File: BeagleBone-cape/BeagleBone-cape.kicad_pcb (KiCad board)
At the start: 4 copper layers, 86.4 x 54.6 mm, 102 parts, among them IC1 A6983C50QTR, IC2 TCAN3413DDFR, IC3 BMP390, J1 Servo 0, J10 MotorR, J11 CAN, J12 24V, J13 MAVLink, J2 Servo 1, J3 Servo 2, J4 Servo 3, J5 LEDL, J6 LEDR, J8 Air Speed Sensor, J9 MotorL, P8 BeagleBone_Black_Header, P9 BeagleBone_Black_Header, Q1 DMP3013SFV, Q2 Q_NMOS_GSD, U1 IIS2MDC, U2 LSM6DSV16X, U3 DS1307ZN+, U4 LSM6DSV16X, U6 LTC4412ES6, Y1 32.768kHz

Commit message: Cape: unify CAN/FDCAN net names in schematic; ISSUES: ERC/DRC status update
Co-Authored-By: Claude Sonnet 5.5 <noreply@anthropic.com>
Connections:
- net /CAN+ renamed /CANH
- net /CAN- renamed /CANL
- P9 pad 14: /IMU_INT2 -> /IMU_INT1
- P9 pad 16: /IMU_INT1 -> /IMU_INT2
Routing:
- net /PGOOD: track 5.02 -> 52.3 mm
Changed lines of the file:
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@@
 	(net 66 "Net-(D1-A)")
 	(net 67 "Net-(D2-A)")
-	(net 68 "/CAN-")
-	(net 69 "/CAN+")
+	(net 68 "/CANL")
+	(net 69 "/CANH")
 	(net 70 "Net-(IC1-VCC)")
 	(net 71 "Net-(IC1-VINLDO)")
@@
 			(layers "*.Cu" "*.Mask")
 			(remove_unused_layers no)
-			(net 94 "/IMU_INT2")
+			(net 92 "/IMU_INT1")
 			(pinfunction "Pin_14")
 			(pintype "passive")
@@
 			(layers "*.Cu" "*.Mask")
 			(remove_unused_layers no)
-			(net 92 "/IMU_INT1")
+			(net 94 "/IMU_INT2")
 			(pinfunction "Pin_16")
 			(pintype "passive")
@@
 			(remove_unused_layers no)
 			(roundrect_rratio 0.125)
-			(net 69 "/CAN+")
+			(net 69 "/CANH")
 			(pinfunction "Pin_1")
 			(pintype "passive")
@@
 			(layers "*.Cu" "*.Mask")
 			(remove_unused_layers no)
-			(net 68 "/CAN-")
+			(net 68 "/CANL")
 			(pinfunction "Pin_2")
 			(pintype "passive")
@@
 			(size 0.45 1.2)
 			(layers "F.Cu" "F.Mask" "F.Paste")
-			(net 68 "/CAN-")
+			(net 68 "/CANL")
 			(pinfunction "CANL")
 			(pintype "passive")
@@
 			(size 0.45 1.2)
 			(layers "F.Cu" "F.Mask" "F.Paste")
-			(net 69 "/CAN+")
+			(net 69 "/CANH")
 			(pinfunction "CANH")
 			(pintype "passive")
@@
 			(layers "F.Cu" "F.Mask" "F.Paste")
 			(roundrect_rratio 0.25)
-			(net 68 "/CAN-")
+			(net 68 "/CANL")
 			(pinfunction "K")
 			(pintype "passive")
@@
 			(layers "F.Cu" "F.Mask" "F.Paste")
 			(roundrect_rratio 0.25)
-			(net 69 "/CAN+")
+			(net 69 "/CANH")
 			(pinfunction "K")
 			(pintype "passive")
@@
 			(size 1 1)
 			(layers "F.Cu" "F.Mask")
-			(net 68 "/CAN-")
+			(net 68 "/CANL")
 			(pinfunction "1")
 			(pintype "passive")
@@
 			(layers "F.Cu" "F.Mask" "F.Paste")
 			(roundrect_rratio 0.25)
-			(net 68 "/CAN-")
+			(net 68 "/CANL")
 			(pintype "passive")
 		)
@@
 			(layers "F.Cu" "F.Mask" "F.Paste")
 			(roundrect_rratio 0.25)
-			(net 69 "/CAN+")
+			(net 69 "/CANH")
 			(pintype "passive")
 		)
@@
 			(size 1 1)
 			(layers "F.Cu" "F.Mask")
-			(net 69 "/CAN+")
+			(net 69 "/CANH")
 			(pinfunction "1")
 			(pintype "passive")
@@
 		(net 101)
 	)
+	(segment
+		(start 123.71 48.58)
+		(end 131.32 48.58)
+		(width 0.25)
+		(layer "In2.Cu")
+		(net 101)
+	)
+	(segment
+		(start 123.49 48.8)
+		(end 123.71 48.58)
+		(width 0.25)
+		(layer "In2.Cu")
+		(net 101)
+	)
+	(segment
+		(start 132.52 47.38)
+		(end 132.5 47.38)
+		(width 0.25)
+		(layer "In2.Cu")
+		(net 101)
+	)
+	(segment
+		(start 121.46 79.15)
+		(end 121.46 54.78)
+		(width 0.25)
+		(layer "In2.Cu")
+		(net 101)
+	)
+	(segment
+		(start 131.32 48.58)
+		(end 132.52 47.38)
+		(width 0.25)
+		(layer "In2.Cu")
+		(net 101)
+	)
+	(segment
+		(start 118.31 82.3)
+		(end 121.46 79.15)
+		(width 0.25)
+		(layer "In2.Cu")
+		(net 101)
+	)
+	(segment
+		(start 123.49 52.75)
+		(end 123.49 48.8)
+		(width 0.25)
+		(layer "In2.Cu")
+		(net 101)
+	)
+	(segment
+		(start 121.46 54.78)
+		(end 123.49 52.75)
+		(width 0.25)
+		(layer "In2.Cu")
+		(net 101)
+	)
+	(segment
+		(start 118.31 84.27)
+		(end 118.31 82.3)
+		(width 0.25)
+		(layer "In2.Cu")
+		(net 101)
+	)

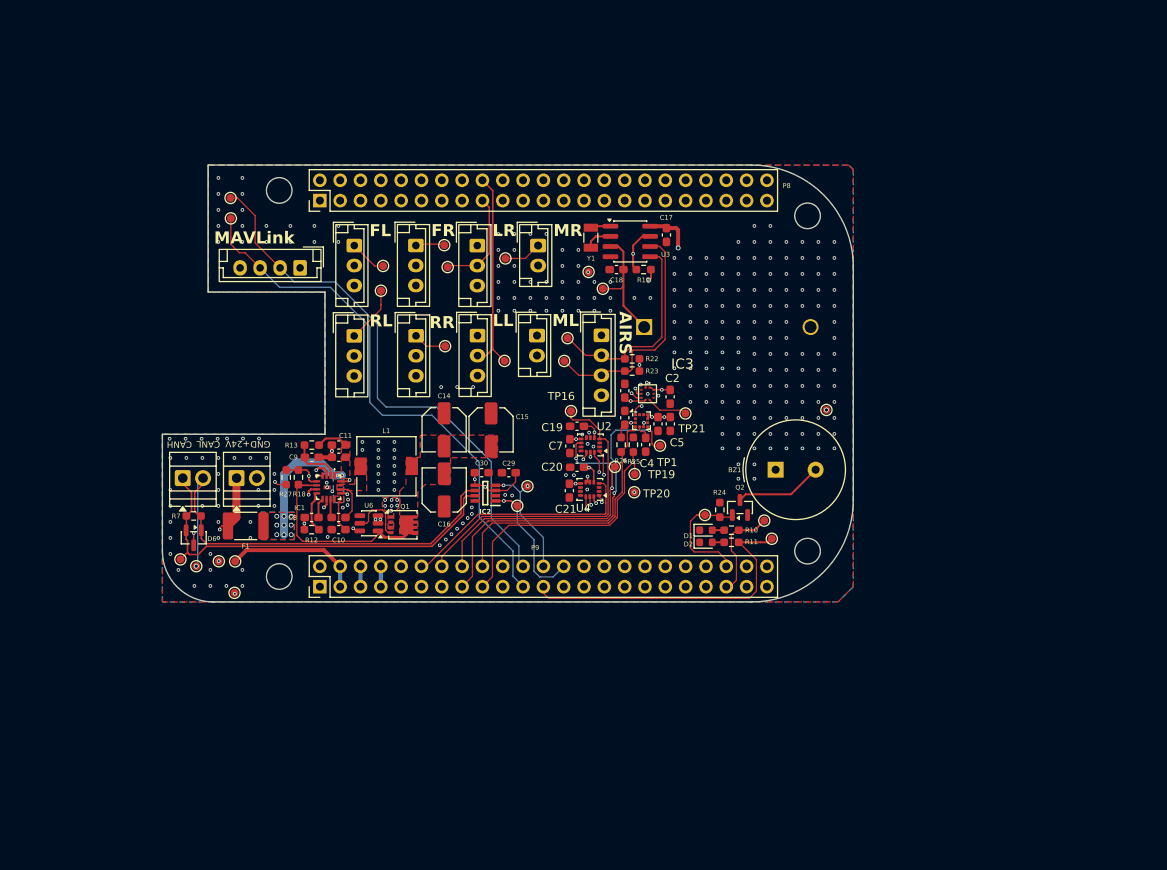
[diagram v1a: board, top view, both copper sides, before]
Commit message: WIP: Q3 -> S-LP03N060TZHG (SOT-223), PCB synced with new schematic parts, not yet routed (DRC: shorts, 200 unconnected)
Co-Authored-By: Claude Sonnet 5.5 <noreply@anthropic.com>
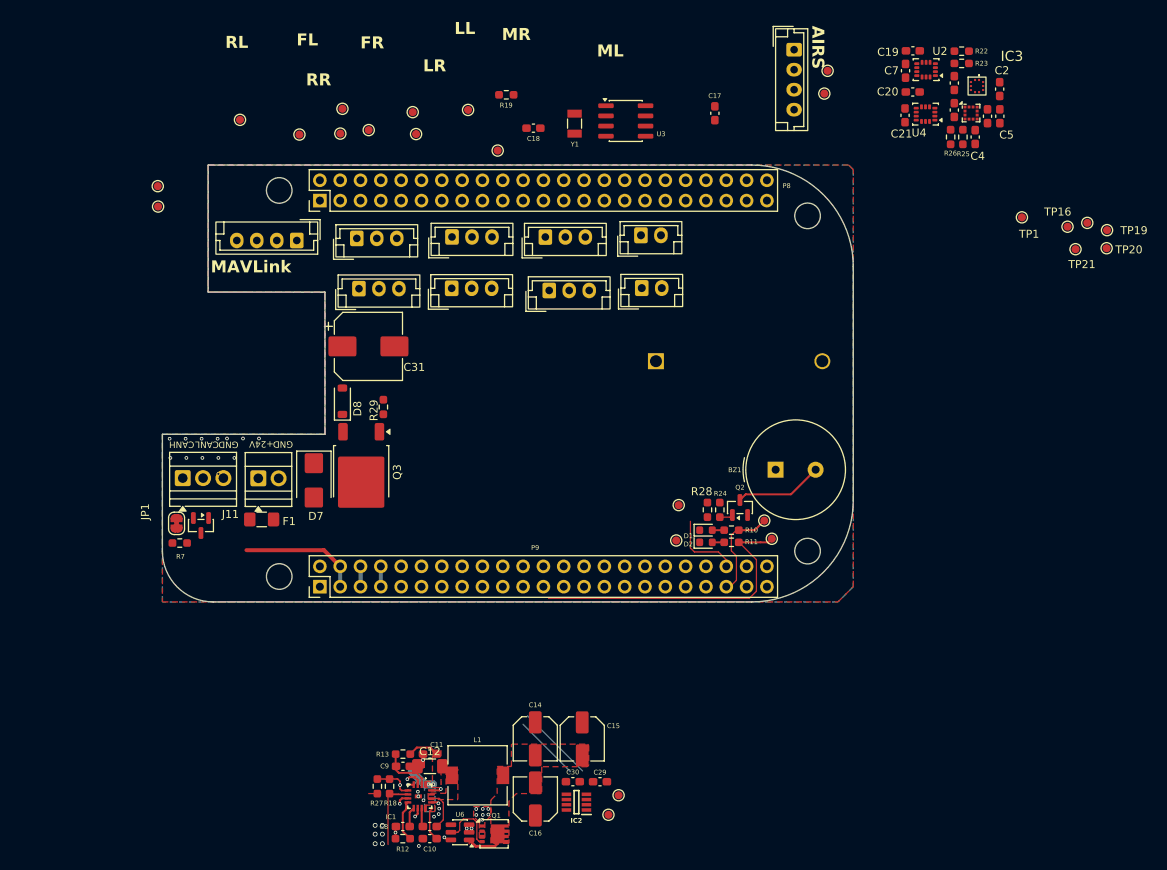
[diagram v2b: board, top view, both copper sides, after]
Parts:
- removed TP10, TP27, TP28, TP29, TP34: TestPoint, TestPoint:TestPoint_Pad_D1.0mm
- added C31: 100u 50V, Capacitor_SMD:CP_Elec_8x10, F.Cu at (125.8, 68.1)
- added D7: SMBJ33CA, Diode_SMD:D_SMB, F.Cu at (118.9, 84.8)
- added D8: BZT52C12, Diode_SMD:D_SOD-123, F.Cu at (122.5, 74.9)
- added JP1: CAN_TERM, Jumper:SolderJumper-2_P1.3mm_Bridged_RoundedPad1.0x1.5mm, F.Cu at (101.8, 90.2)
- added Q3: AOD4185L, Package_TO_SOT_SMD:TO-252-2, F.Cu at (124.8, 83.8)
- added R28: 1k, Resistor_SMD:R_0603_1608Metric_Pad0.98x0.95mm_HandSolder, F.Cu at (168.1, 88.5)
- added R29: 100k, Resistor_SMD:R_0603_1608Metric_Pad0.98x0.95mm_HandSolder, F.Cu at (127.6, 75.6)
- C12: value 10u -> 10u 50V; footprint Capacitor_SMD:C_0603_1608Metric_Pad1.08x0.95mm_HandSolder -> Capacitor_SMD:C_1206_3216Metric_Pad1.33x1.80mm_HandSolder
- F1: value Fuse -> 2A 63V; footprint Fuse:Fuse_1812_4532Metric_Pad1.30x3.40mm_HandSolder -> Fuse:Fuse_1206_3216Metric_Pad1.42x1.75mm_HandSolder
- J11: footprint TerminalBlock:TerminalBlock_Xinya_XY308-2.54-2P_1x02_P2.54mm_Horizontal -> TerminalBlock:TerminalBlock_Xinya_XY308-2.54-3P_1x03_P2.54mm_Horizontal
- J2: value Servo 1 -> Servo 2
- J3: value Servo 2 -> Servo 1
- R10: value 420 -> 100
- R11: value 420 -> 470
- moved TP17 66.5 mm to (215.6, 52.6)
- moved TP19 66.5 mm to (218.1, 53.5)
- moved TP20 66.5 mm to (218.0, 55.8)
- moved TP16 66.2 mm to (213.1, 53.1)
- moved C19 63.0 mm to (193.8, 31.1)
- moved C21 62.9 mm to (192.8, 39.2)
- moved C7 62.9 mm to (192.9, 33.6)
- moved U2 62.9 mm to (195.5, 33.5)
- moved C20 62.9 mm to (193.8, 36.3)
- moved U4 62.9 mm to (195.4, 39.0)
- moved IC3 56.4 mm to (201.8, 35.5)
- moved C1 56.4 mm to (199.0, 35.1)
- moved C2 56.4 mm to (204.7, 35.9)
- moved C3 56.4 mm to (203.1, 39.3)
- moved C4 56.4 mm to (201.6, 41.9)
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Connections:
- net /FDCAN_RX renamed /CAN_RX
- net /FDCAN_TX renamed /CAN_TX
- F1 pad 2: +24V -> /Power/VIN_F
- R7 pad 2: /CANH -> Net-(JP1-B)
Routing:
- net /SERVO_1: track 68.9 -> 0.00 mm
- net /I2C2.SCL: track 64.2 -> 0.00 mm
- net /SERVO_3: track 61.8 -> 0.00 mm
- net /UART_TX: track 68.9 -> 8.39 mm
- net /I2C2.SDA: track 59.2 -> 0.00 mm
- net /UART_RX: track 68.4 -> 9.70 mm
- net /CANL: track 58.5 -> 0.00 mm, vias 1 -> 0
- net /SERVO_0: track 52.4 -> 0.00 mm
- net /CANH: track 52.0 -> 0.00 mm
- net /I2C1.SDA: track 50.1 -> 0.00 mm, vias 3 -> 0
- net /I2C1.SCL: track 47.2 -> 0.00 mm, vias 3 -> 0
- net /SERVO_2: track 46.2 -> 0.00 mm
- net /PGOOD: track 52.3 -> 6.99 mm
- net /MAG_DRDY: track 44.5 -> 0.00 mm, vias 2 -> 0
- net /MOTOR_R: track 41.4 -> 0.00 mm
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
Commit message: WIP: snap servo/LED/motor connectors to 4x2 grid, further PCB and pwr sheet edits
Co-Authored-By: Claude Sonnet 5.5 <noreply@anthropic.com>
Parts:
- removed C12: 10u 50V, Capacitor_SMD:C_1206_3216Metric_Pad1.33x1.80mm_HandSolder
- added TP10: TestPoint, TestPoint:TestPoint_Pad_D1.0mm, F.Cu at (83.8, 79.9)
- added TP27: TestPoint, TestPoint:TestPoint_Pad_D1.0mm, F.Cu at (83.8, 82.9)
- added TP28: TestPoint, TestPoint:TestPoint_Pad_D1.0mm, F.Cu at (83.8, 86.0)
- added TP29: TestPoint, TestPoint:TestPoint_Pad_D1.0mm, F.Cu at (83.8, 89.0)
- added TP34: TestPoint, TestPoint:TestPoint_Pad_D1.0mm, F.Cu at (83.8, 92.1)
- Q3: value AOD4185L -> S-LP03N060TZHG; footprint Package_TO_SOT_SMD:TO-252-2 -> Package_TO_SOT_SMD:SOT-223-3_TabPin2
- moved C3 83.1 mm to (131.9, 82.1), turned to 180 degrees
- moved C4 79.7 mm to (131.9, 80.5), turned to 180 degrees
- moved U4 79.0 mm to (131.9, 86.2), turned to 90 degrees
- moved U2 78.7 mm to (137.0, 86.2), turned to 90 degrees
- moved IC3 77.7 mm to (138.3, 80.3), turned to -90 degrees
- moved U1 77.7 mm to (134.9, 79.5), turned to -90 degrees
- moved R25 77.6 mm to (131.9, 79.0), turned to 180 degrees
- moved C2 77.1 mm to (142.1, 80.9), turned to 0 degrees
- moved C20 76.6 mm to (134.4, 84.5), turned to 90 degrees
- moved C19 76.3 mm to (139.3, 84.5), turned to 90 degrees
- moved R26 75.5 mm to (131.9, 77.5), turned to 180 degrees
- moved C21 75.4 mm to (131.9, 83.6), turned to 180 degrees
- moved C7 75.1 mm to (136.8, 83.6), turned to 180 degrees
- moved C6 74.7 mm to (135.3, 77.5), turned to 0 degrees
- moved R23 74.5 mm to (141.1, 78.4), turned to 90 degrees
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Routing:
- net +3V3: track 16.3 -> 2.67 mm
- net /UART_RX: track 9.70 -> 0.00 mm
- net /UART_TX: track 8.39 -> 0.00 mm
- net /Power/BUCK_OUT: track 15.5 -> 8.17 mm
- net Net-(IC1-VINLDO): track 6.11 -> 0.80 mm
- net GND: track 11.7 -> 6.97 mm, vias 28 -> 26
- net +24V: track 16.0 -> 12.0 mm, vias 9 -> 3
- net /PGOOD: track 6.99 -> 3.53 mm
- net /SYS_5V: track 3.99 -> 2.54 mm
- net +5V: track 5.02 -> 4.07 mm, vias 9 -> 1
- removed copper zone on F.Cu, net +5V
- removed copper zone on F.Cu, net /Power/BUCK_OUT
